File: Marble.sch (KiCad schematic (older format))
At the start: 16 parts

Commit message: 16 warnings, 16 errors
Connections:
- net labels removed: I2C_PM_SCL, I2C_PM_SDA
- wire segments 356 -> 354
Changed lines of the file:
@@
 F8 "DDR3_RST_N" B L 14150 5150 50
 F9 "PGOOD" B L 14150 2050 50
-F10 "I2C_DDR3_SDA" B R 15650 3250 50
-F11 "I2C_DDR3_SCL" I R 15650 3350 50
 F12 "DDR3_CS_N" B L 14150 5050 50
 F13 "DDR3_RAS_N" B L 14150 5250 50
@@
 F0 "ETH_PHY" 50
 F1 "ETH_PHY.sch" 50
-F2 "SD_OUT_N" I L 8400 4050 50
-F3 "SD_OUT_P" I L 8400 4150 50
-F4 "SD_IN_N" I L 8400 4300 50
-F5 "SD_IN_P" I L 8400 4400 50
 F6 "MII_MDIO" I L 8400 4650 50
 F7 "MII_MDC" I L 8400 4750 50
@@
 F122 "I2C_CLKMUX_SCL" I L 11350 5300 50
 F123 "I2C_CLKMUX_SDA" B L 11350 5400 50
-F124 "CLKMUX_RST" I L 11350 5500 50
 F125 "DDR3_DQ[32..63]" B R 12950 2300 50
 F126 "DDR3_DQS4_P" B R 12950 3500 50
@@
 Wire Wire Line
 	12950 4700 14150 4700
-Wire Wire Line
-	15650 3250 16300 3250
-Text Label 15800 3250 0    50   ~ 10
-I2C_PM_SDA
-Text Label 15800 3350 0    50   ~ 10
-I2C_PM_SCL
-Wire Wire Line
-	16300 3350 15650 3350
 Wire Notes Line
 	12950 6950 12300 6950

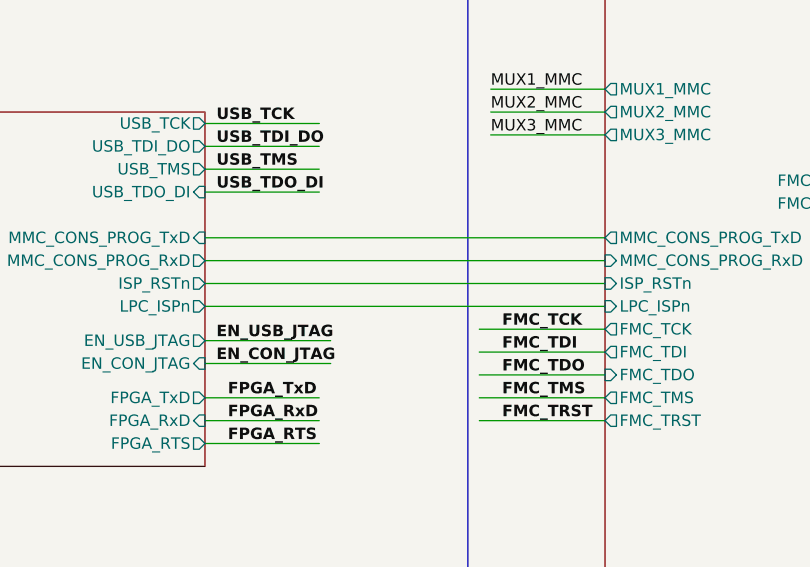
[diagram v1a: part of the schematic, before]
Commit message: shave ERC report down to 5 issues
  * mostly by adding power inputs / outputs to the symbols (many
    power pins were set to bidirectional, which causes issues)
  * remove some stray power symbols which were not connected to
    anything
  * FMC connector: change all VCC and GND pins to Power input type
    (there's a lot of them!!)
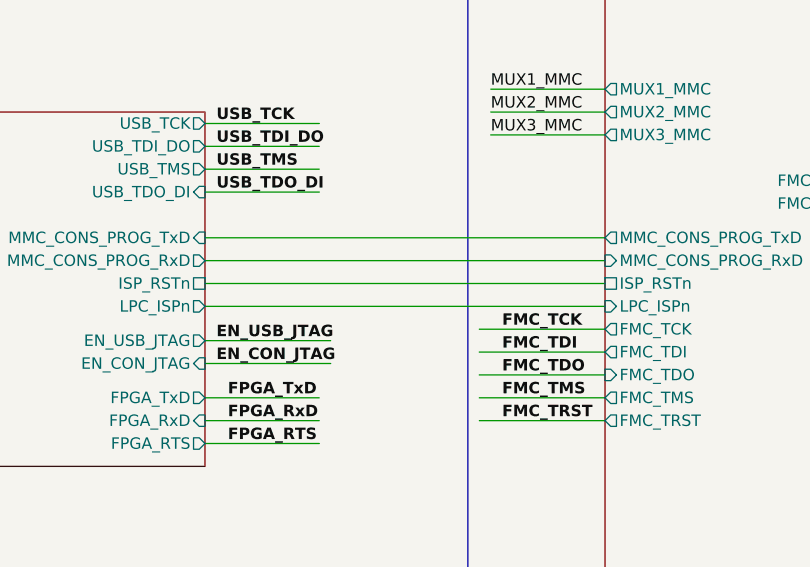
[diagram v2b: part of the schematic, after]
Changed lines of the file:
@@
 F8 "DDR3_RST_N" B L 14150 5150 50
 F9 "PGOOD" B L 14150 2050 50
-F12 "DDR3_CS_N" B L 14150 5050 50
-F13 "DDR3_RAS_N" B L 14150 5250 50
-F14 "DDR3_CAS_N" B L 14150 5350 50
-F15 "DDR3_WE_N" B L 14150 5450 50
-F16 "DDR3_DM[4..7]" B L 14150 2550 50
-F17 "DDR3_DQ[32..63]" B L 14150 2300 50
-F18 "DDR3_DQS4_P" B L 14150 3500 50
-F19 "DDR3_DQS4_N" B L 14150 3600 50
-F20 "DDR3_DQS5_P" B L 14150 3700 50
-F21 "DDR3_DQS5_N" B L 14150 3800 50
-F22 "DDR3_DQS6_P" B L 14150 3900 50
-F23 "DDR3_DQS6_N" B L 14150 4000 50
-F24 "DDR3_DQS7_P" B L 14150 4100 50
-F25 "DDR3_DQS7_N" B L 14150 4200 50
-F26 "DDR3_DQ[0..31]" B L 14150 2200 50
-F27 "DDR3_DM[0..3]" B L 14150 2450 50
-F28 "DDR3_DQS0_P" B L 14150 2700 50
-F29 "DDR3_DQS0_N" B L 14150 2800 50
-F30 "DDR3_DQS1_P" B L 14150 2900 50
-F31 "DDR3_DQS1_N" B L 14150 3000 50
-F32 "DDR3_DQS2_P" B L 14150 3100 50
-F33 "DDR3_DQS2_N" B L 14150 3200 50
-F34 "DDR3_DQS3_P" B L 14150 3300 50
-F35 "DDR3_DQS3_N" B L 14150 3400 50
-F36 "VREF_DDR3" O L 14150 5600 50
+F10 "DDR3_CS_N" B L 14150 5050 50
+F11 "DDR3_RAS_N" B L 14150 5250 50
+F12 "DDR3_CAS_N" B L 14150 5350 50
+F13 "DDR3_WE_N" B L 14150 5450 50
+F14 "DDR3_DM[4..7]" B L 14150 2550 50
+F15 "DDR3_DQ[32..63]" B L 14150 2300 50
+F16 "DDR3_DQS4_P" B L 14150 3500 50
+F17 "DDR3_DQS4_N" B L 14150 3600 50
+F18 "DDR3_DQS5_P" B L 14150 3700 50
+F19 "DDR3_DQS5_N" B L 14150 3800 50
+F20 "DDR3_DQS6_P" B L 14150 3900 50
+F21 "DDR3_DQS6_N" B L 14150 4000 50
+F22 "DDR3_DQS7_P" B L 14150 4100 50
+F23 "DDR3_DQS7_N" B L 14150 4200 50
+F24 "DDR3_DQ[0..31]" B L 14150 2200 50
+F25 "DDR3_DM[0..3]" B L 14150 2450 50
+F26 "DDR3_DQS0_P" B L 14150 2700 50
+F27 "DDR3_DQS0_N" B L 14150 2800 50
+F28 "DDR3_DQS1_P" B L 14150 2900 50
+F29 "DDR3_DQS1_N" B L 14150 3000 50
+F30 "DDR3_DQS2_P" B L 14150 3100 50
+F31 "DDR3_DQS2_N" B L 14150 3200 50
+F32 "DDR3_DQS3_P" B L 14150 3300 50
+F33 "DDR3_DQS3_N" B L 14150 3400 50
+F34 "VREF_DDR3" O L 14150 5600 50
 $EndSheet
 $Sheet
@@
 F0 "USB" 50
 F1 "USB.sch" 50
-F2 "ISP_RSTn" O R 3450 8000 50
-F3 "LPC_ISPn" O R 3450 8100 50
-F4 "EN_USB_JTAG" O R 3450 8250 50
-F5 "USB_TCK" O R 3450 7300 50
-F6 "USB_TDI_DO" O R 3450 7400 50
-F7 "USB_TMS" O R 3450 7500 50
-F8 "USB_TDO_DI" I R 3450 7600 50
-F9 "MMC_CONS_PROG_TxD" I R 3450 7800 50
-F10 "MMC_CONS_PROG_RxD" O R 3450 7900 50
-F11 "EN_CON_JTAG" I R 3450 8350 50
-F12 "FPGA_TxD" O R 3450 8500 50
-F13 "FPGA_RxD" I R 3450 8600 50
-F14 "FPGA_RTS" O R 3450 8700 50
+F2 "LPC_ISPn" O R 3450 8100 50
+F3 "EN_USB_JTAG" O R 3450 8250 50
+F4 "USB_TCK" O R 3450 7300 50
+F5 "USB_TDI_DO" O R 3450 7400 50
+F6 "USB_TMS" O R 3450 7500 50
+F7 "USB_TDO_DI" I R 3450 7600 50
+F8 "MMC_CONS_PROG_TxD" I R 3450 7800 50
+F9 "MMC_CONS_PROG_RxD" O R 3450 7900 50
+F10 "EN_CON_JTAG" I R 3450 8350 50
+F11 "FPGA_TxD" O R 3450 8500 50
+F12 "FPGA_RxD" I R 3450 8600 50
+F13 "FPGA_RTS" O R 3450 8700 50
+F14 "ISP_RSTn" U R 3450 8000 50
 $EndSheet
 Wire Wire Line
@@
 F13 "EN_PSU_CH" O L 5200 9450 50
 F14 "EN_FMC2_P12V" O L 5200 9550 50
-F15 "ISP_RSTn" I L 5200 8000 50
-F16 "I2C_PM_SDA" B L 5200 10150 50
-F17 "I2C_PM_SCL" O L 5200 10250 50
-F18 "CLK_25MHZ" I R 6800 7450 50
-F19 "FPGA_SCK" I R 6800 10050 50
-F20 "FPGA_SSEL" I R 6800 10150 50
-F21 "FPGA_MISO" I R 6800 10250 50
-F22 "FPGA_MOSI" I R 6800 10350 50
-F23 "OVER_TEMP" I L 5200 9300 50
-F24 "MII_MDIO" I R 6800 6850 50
-F25 "MII_MDC" I R 6800 6950 50
-F26 "AT_DET" I L 5200 9750 50
-F27 "FPGA_INT" I R 6800 9950 50
-F28 "PROG_B" I R 6800 9750 50
-F29 "FPGA_DONE" I R 6800 9850 50
-F30 "LPC_RST" I R 6800 8650 50
-F31 "MMC_TCK" I R 6800 8750 50
-F32 "MMC_TMS" I R 6800 8850 50
-F33 "MMC_TDO" O R 6800 8950 50
-F34 "MMC_TDI" I R 6800 9050 50
-F35 "Pmod3_[0..7]" I R 6800 9450 50
-F36 "FMC1_FUSE" I R 6800 7300 50
-F37 "FMC2_FUSE" I R 6800 9150 50
-F38 "FMC_TCK" O L 5200 8200 50
-F39 "FMC_TDI" O L 5200 8300 50
-F40 "FMC_TDO" I L 5200 8400 50
-F41 "FMC_TMS" O L 5200 8500 50
-F42 "FMC_TRST" O L 5200 8600 50
-F43 "FMC1_PRSNT_Override" O R 6800 7550 50
-F44 "FMC2_PRSNT_Override" O R 6800 7650 50
-F45 "MUX1_MMC" O L 5200 7150 50
-F46 "MUX2_MMC" O L 5200 7250 50
-F47 "MUX3_MMC" O L 5200 7350 50
+F15 "I2C_PM_SDA" B L 5200 10150 50
+F16 "I2C_PM_SCL" O L 5200 10250 50
+F17 "CLK_25MHZ" I R 6800 7450 50
+F18 "FPGA_SCK" I R 6800 10050 50
+F19 "FPGA_SSEL" I R 6800 10150 50
+F20 "FPGA_MISO" I R 6800 10250 50
+F21 "FPGA_MOSI" I R 6800 10350 50
+F22 "OVER_TEMP" I L 5200 9300 50
+F23 "MII_MDIO" I R 6800 6850 50
+F24 "MII_MDC" I R 6800 6950 50
+F25 "AT_DET" I L 5200 9750 50
+F26 "FPGA_INT" I R 6800 9950 50
+F27 "PROG_B" I R 6800 9750 50
+F28 "FPGA_DONE" I R 6800 9850 50
+F29 "LPC_RST" I R 6800 8650 50
+F30 "MMC_TCK" I R 6800 8750 50
+F31 "MMC_TMS" I R 6800 8850 50
+F32 "MMC_TDO" O R 6800 8950 50
+F33 "MMC_TDI" I R 6800 9050 50
+F34 "Pmod3_[0..7]" I R 6800 9450 50
+F35 "FMC1_FUSE" I R 6800 7300 50
+F36 "FMC2_FUSE" I R 6800 9150 50
+F37 "FMC_TCK" O L 5200 8200 50
+F38 "FMC_TDI" O L 5200 8300 50
+F39 "FMC_TDO" I L 5200 8400 50
+F40 "FMC_TMS" O L 5200 8500 50
+F41 "FMC_TRST" O L 5200 8600 50
+F42 "FMC1_PRSNT_Override" O R 6800 7550 50
+F43 "FMC2_PRSNT_Override" O R 6800 7650 50
+F44 "MUX1_MMC" O L 5200 7150 50
+F45 "MUX2_MMC" O L 5200 7250 50
+F46 "MUX3_MMC" O L 5200 7350 50
+F47 "ISP_RSTn" U L 5200 8000 50
 $EndSheet
 Text Label 6800 7550 0    50   ~ 10
@@
 F0 "ETH_PHY" 50
 F1 "ETH_PHY.sch" 50
-F6 "MII_MDIO" I L 8400 4650 50
-F7 "MII_MDC" I L 8400 4750 50
-F8 "PHY_RSTn" I R 10050 4200 50
-F9 "RGMII_RXD[0..3]" I R 10050 4300 50
-F10 "RGMII_TXD[0..3]" I R 10050 4400 50
-F11 "RGMII_TX_EN" I R 10050 4500 50
-F12 "RGMII_TX_CLK" I R 10050 4600 50
-F13 "RGMII_RX_DV" I R 10050 4700 50
-F14 "RGMII_RX_CLK" I R 10050 4800 50
-F15 "POE_VC[1..4]" I L 8400 4850 50
-F16 "CLK_25MHZ" I L 8400 4550 50
+F2 "MII_MDIO" I L 8400 4650 50
+F3 "MII_MDC" I L 8400 4750 50
+F4 "PHY_RSTn" I R 10050 4200 50
+F5 "RGMII_RXD[0..3]" I R 10050 4300 50
+F6 "RGMII_TXD[0..3]" I R 10050 4400 50
+F7 "RGMII_TX_EN" I R 10050 4500 50
+F8 "RGMII_TX_CLK" I R 10050 4600 50
+F9 "RGMII_RX_DV" I R 10050 4700 50
+F10 "RGMII_RX_CLK" I R 10050 4800 50
+F11 "POE_VC[1..4]" I L 8400 4850 50
+F12 "CLK_25MHZ" I L 8400 4550 50
 $EndSheet
 Text Notes 2500 2500 0    394  ~ 79
@@
 F122 "I2C_CLKMUX_SCL" I L 11350 5300 50
 F123 "I2C_CLKMUX_SDA" B L 11350 5400 50
-F125 "DDR3_DQ[32..63]" B R 12950 2300 50
-F126 "DDR3_DQS4_P" B R 12950 3500 50
-F127 "DDR3_DQS4_N" B R 12950 3600 50
-F128 "DDR3_DQS5_P" B R 12950 3700 50
-F129 "DDR3_DQS5_N" B R 12950 3800 50
-F130 "DDR3_DQS6_P" B R 12950 3900 50
-F131 "DDR3_DQS6_N" B R 12950 4000 50
-F132 "DDR3_DQS7_P" B R 12950 4100 50
-F133 "DDR3_DQS7_N" B R 12950 4200 50
-F134 "DDR3_DM[4..7]" B R 12950 2550 50
-F135 "DDR3_RAS_N" B R 12950 5250 50
-F136 "DDR3_CAS_N" B R 12950 5350 50
-F137 "DDR3_WE_N" B R 12950 5450 50
-F138 "DDR3_CS_N" B R 12950 5050 50
-F139 "DDR3_DQS0_P" B R 12950 2700 50
-F140 "DDR3_DQS0_N" B R 12950 2800 50
-F141 "DDR3_DQS1_P" B R 12950 2900 50
-F142 "DDR3_DQS1_N" B R 12950 3000 50
-F143 "DDR3_DQS2_P" B R 12950 3100 50
-F144 "DDR3_DQS2_N" B R 12950 3200 50
-F145 "DDR3_DQS3_P" B R 12950 3300 50
-F146 "DDR3_DQS3_N" B R 12950 3400 50
-F147 "DDR3_DM[0..3]" B R 12950 2450 50
-F148 "DDR3_DQ[0..31]" B R 12950 2200 50
-F149 "VREF_DDR3" I R 12950 5600 50
-F150 "SI570_OE" O L 11350 5600 50
+F124 "DDR3_DQ[32..63]" B R 12950 2300 50
+F125 "DDR3_DQS4_P" B R 12950 3500 50
+F126 "DDR3_DQS4_N" B R 12950 3600 50
+F127 "DDR3_DQS5_P" B R 12950 3700 50
+F128 "DDR3_DQS5_N" B R 12950 3800 50
+F129 "DDR3_DQS6_P" B R 12950 3900 50
+F130 "DDR3_DQS6_N" B R 12950 4000 50
+F131 "DDR3_DQS7_P" B R 12950 4100 50
+F132 "DDR3_DQS7_N" B R 12950 4200 50
+F133 "DDR3_DM[4..7]" B R 12950 2550 50
+F134 "DDR3_RAS_N" B R 12950 5250 50
+F135 "DDR3_CAS_N" B R 12950 5350 50
+F136 "DDR3_WE_N" B R 12950 5450 50
+F137 "DDR3_CS_N" B R 12950 5050 50
+F138 "DDR3_DQS0_P" B R 12950 2700 50
+F139 "DDR3_DQS0_N" B R 12950 2800 50
+F140 "DDR3_DQS1_P" B R 12950 2900 50
+F141 "DDR3_DQS1_N" B R 12950 3000 50
+F142 "DDR3_DQS2_P" B R 12950 3100 50
+F143 "DDR3_DQS2_N" B R 12950 3200 50
+F144 "DDR3_DQS3_P" B R 12950 3300 50
+F145 "DDR3_DQS3_N" B R 12950 3400 50
+F146 "DDR3_DM[0..3]" B R 12950 2450 50
+F147 "DDR3_DQ[0..31]" B R 12950 2200 50
+F148 "VREF_DDR3" I R 12950 5600 50
+F149 "SI570_OE" O L 11350 5600 50
 $EndSheet
 Wire Notes Line

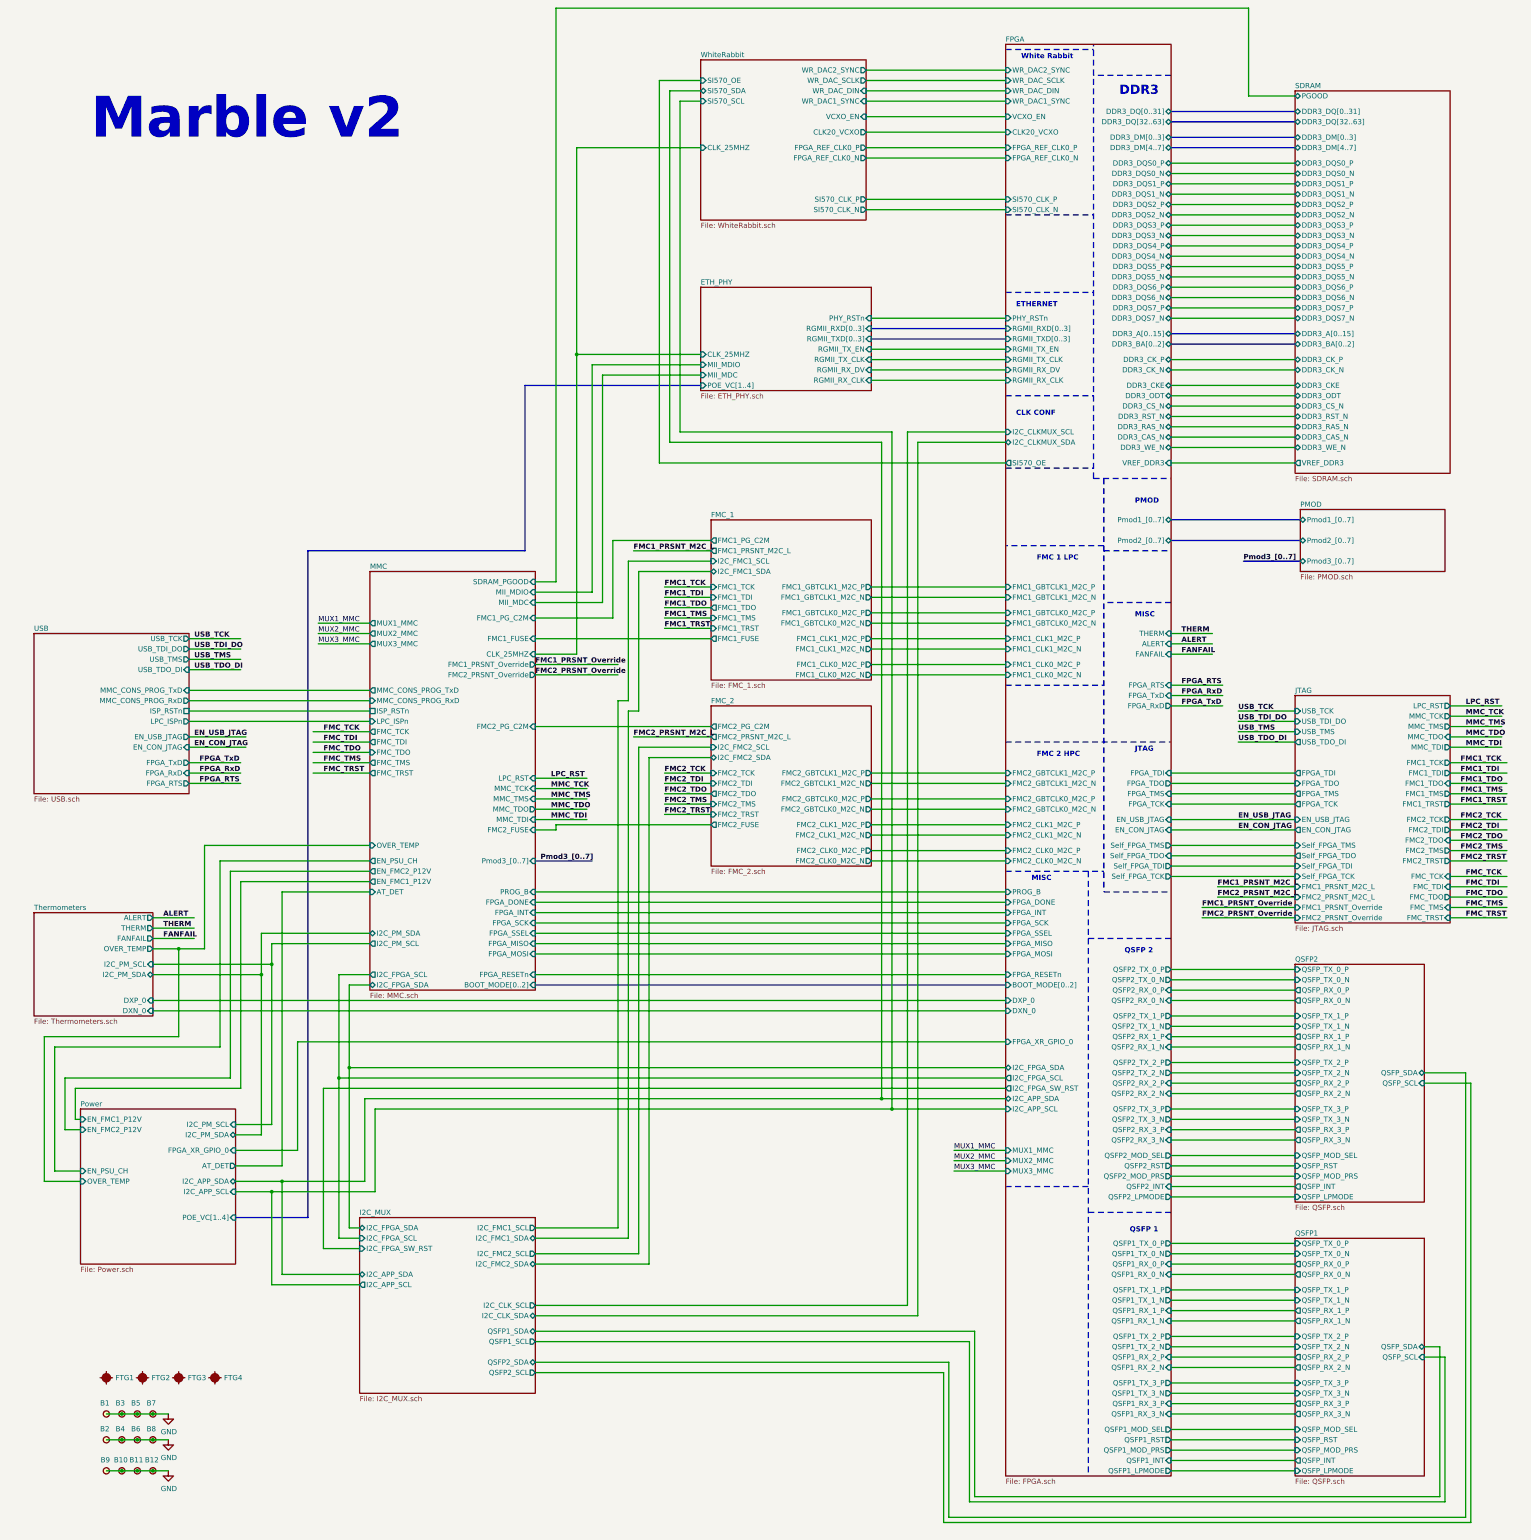
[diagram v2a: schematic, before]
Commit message: I2C voltage translator added, rotated POE bridges, I2C connected to SODIMM, NMOS for power leds indicator, 3V3P connected to SI570 and SODIMM
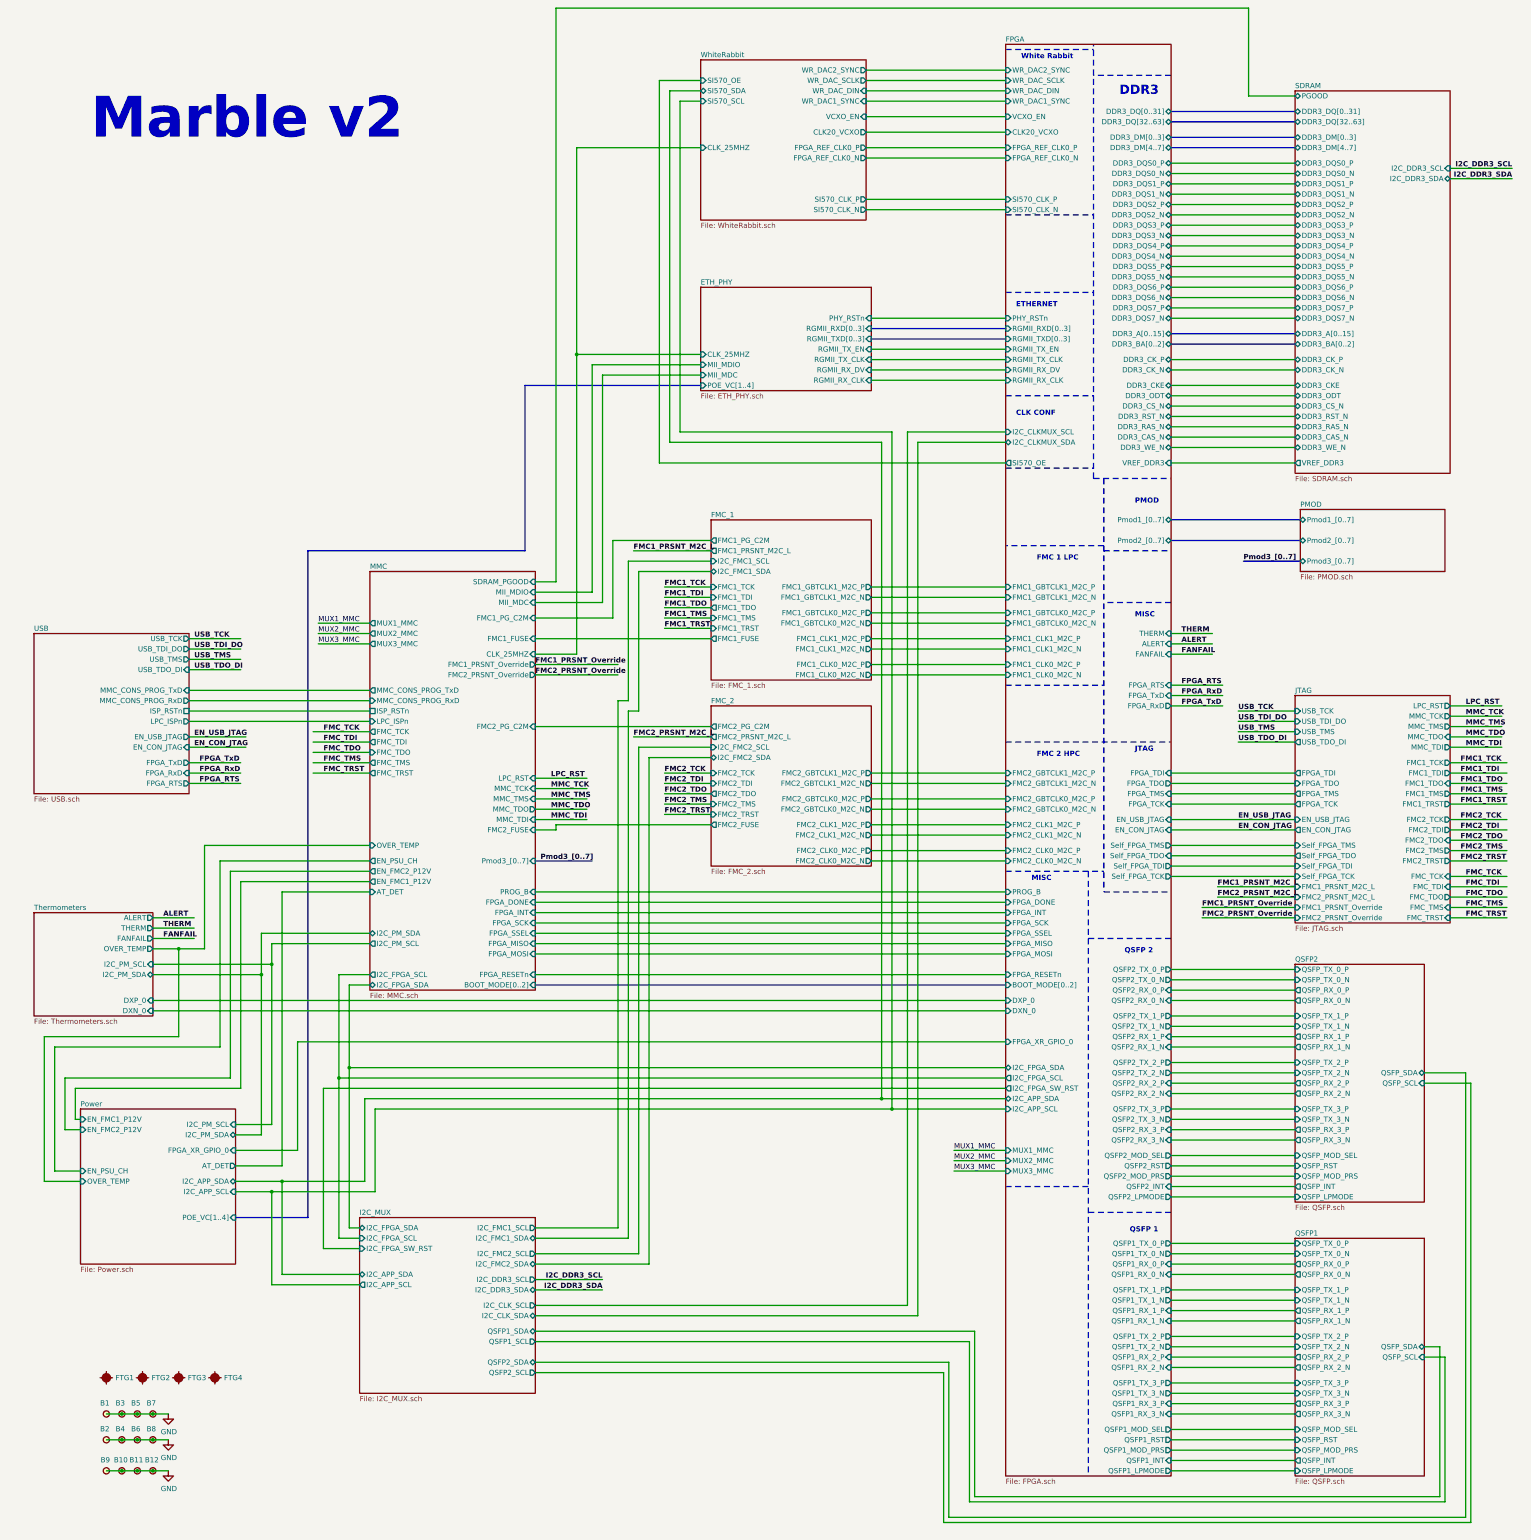
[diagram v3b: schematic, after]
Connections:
- net labels added: I2C_DDR3_SCL, I2C_DDR3_SDA
- wire segments 354 -> 358
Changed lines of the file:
@@
 F33 "DDR3_DQS3_N" B L 14150 3400 50
 F34 "VREF_DDR3" O L 14150 5600 50
+F35 "I2C_DDR3_SDA" B R 15650 2850 50
+F36 "I2C_DDR3_SCL" I R 15650 2750 50
 $EndSheet
 $Sheet
@@
 F15 "I2C_CLK_SCL" O R 6800 13750 50
 F16 "I2C_CLK_SDA" B R 6800 13850 50
+F17 "I2C_DDR3_SDA" B R 6800 13600 50
+F18 "I2C_DDR3_SCL" O R 6800 13500 50
 $EndSheet
 Wire Wire Line
@@
 Wire Wire Line
 	10250 11850 5250 11850
+Wire Wire Line
+	7450 13500 6800 13500
+Wire Wire Line
+	7450 13600 6800 13600
+Text Label 7450 13500 2    50   ~ 10
+I2C_DDR3_SCL
+Text Label 7450 13600 2    50   ~ 10
+I2C_DDR3_SDA
+Text Label 16250 2750 2    50   ~ 10
+I2C_DDR3_SCL
+Text Label 16250 2850 2    50   ~ 10
+I2C_DDR3_SDA
+Wire Wire Line
+	16250 2750 15650 2750
+Wire Wire Line
+	16250 2850 15650 2850
 $EndSCHEMATC
